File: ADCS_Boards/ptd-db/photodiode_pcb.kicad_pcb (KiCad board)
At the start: 2 copper layers, 16.5 x 5.1 mm, 3 parts

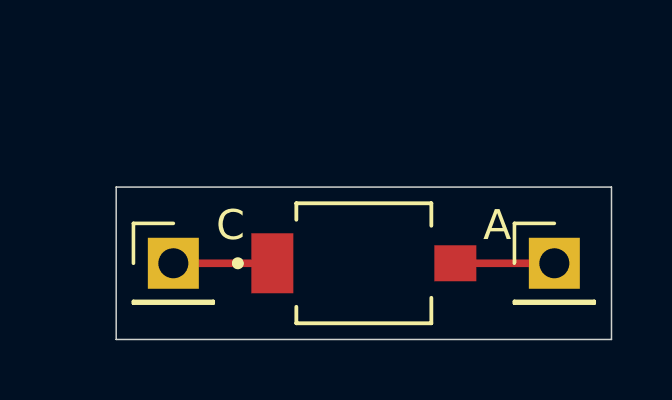
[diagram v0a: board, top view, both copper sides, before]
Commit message: adcs: ptd-db: added silksreens
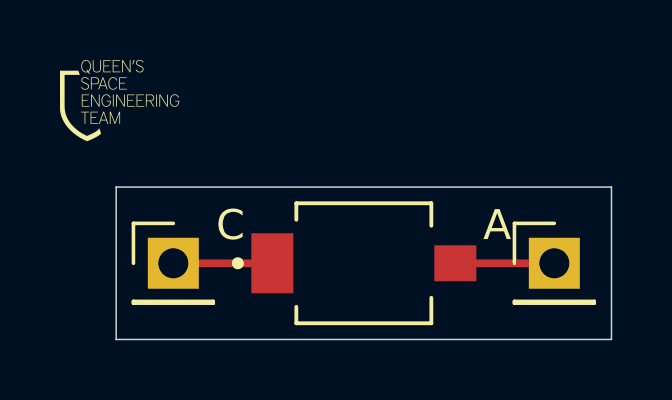
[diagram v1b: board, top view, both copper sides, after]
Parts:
- added G***: LOGO, LOGO, F.Cu at (136.0, 99.9)
- added G***: LOGO, LOGO, B.Cu at (148.0, 105.0)
- added G***: LOGO, LOGO, B.Cu at (140.3, 104.9)
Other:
- net class Default removed
- board text added: "Alex Macquarrie"
- board text added: "PTD-DB-REV-A"

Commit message: adcs: ptd-db: deleted floating silkscreen
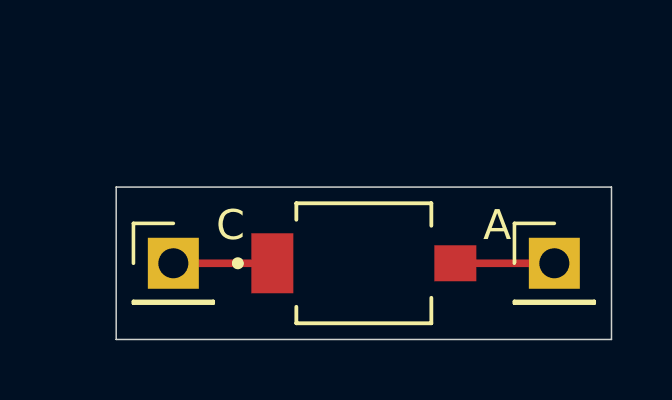
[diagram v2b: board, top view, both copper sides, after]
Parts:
- removed the G*** at (136.0, 99.9)
